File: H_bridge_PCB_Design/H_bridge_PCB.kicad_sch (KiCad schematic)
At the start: 7 parts, among them U1 ESP32-WROOM-32

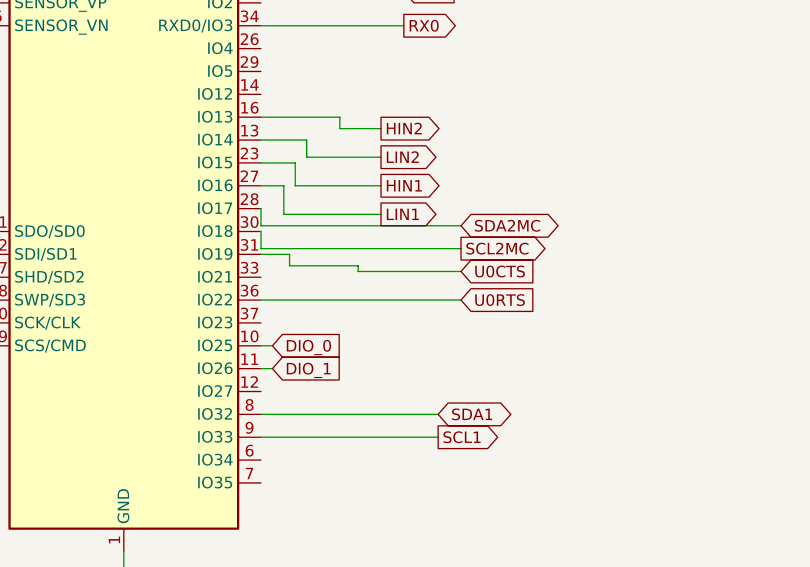
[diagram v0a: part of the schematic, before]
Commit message: Interrupt for PWM and unipolar modulation
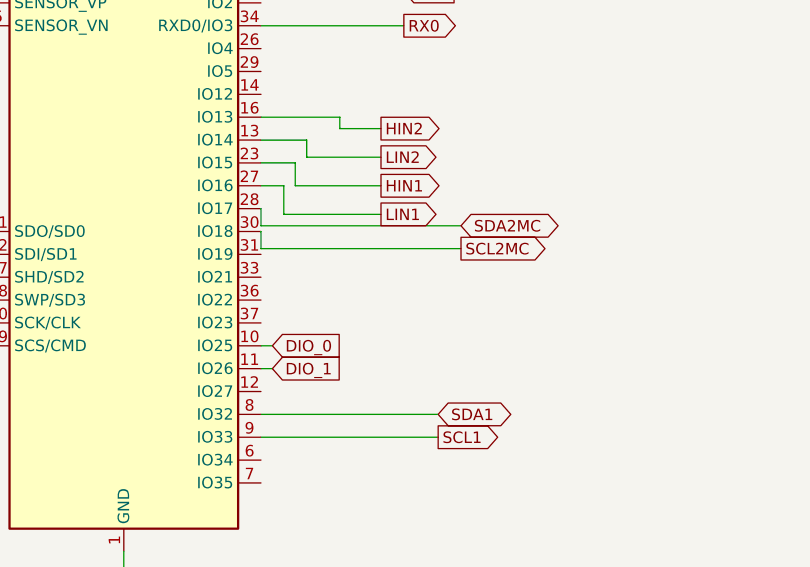
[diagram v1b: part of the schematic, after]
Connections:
- net U0CTS: no longer names the net of U1.31 (IO19)
- net U0RTS: no longer names the net of U1.36 (IO22)
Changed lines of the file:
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@@
-	(wire
-		(pts
-			(xy 208.915 217.805) (xy 208.915 218.44)
-		)
-		(stroke
-			(width 0)
-			(type default)
-		)
-	)
 	(wire
 		(pts
@@
 	(wire
 		(pts
-			(xy 201.295 217.805) (xy 208.915 217.805)
-		)
-		(stroke
-			(width 0)
-			(type default)
-		)
-	)
-	(wire
-		(pts
 			(xy 154.94 183.515) (xy 167.64 183.515)
 		)
@@
 	(wire
 		(pts
-			(xy 198.12 216.535) (xy 201.295 216.535)
-		)
-		(stroke
-			(width 0)
-			(type default)
-		)
-	)
-	(wire
-		(pts
-			(xy 208.915 218.44) (xy 220.345 218.44)
-		)
-		(stroke
-			(width 0)
-			(type default)
-		)
-	)
-	(wire
-		(pts
 			(xy 166.37 175.26) (xy 166.37 176.53)
 		)
@@
 	(wire
 		(pts
-			(xy 201.295 216.535) (xy 201.295 217.805)
-		)
-		(stroke
-			(width 0)
-			(type default)
-		)
-	)
-	(wire
-		(pts
 			(xy 198.12 186.055) (xy 206.375 186.055)
 		)
@@
 		(pts
 			(xy 203.2 205.74) (xy 203.2 203.835)
-		)
-		(stroke
-			(width 0)
-			(type default)
-		)
-	)
-	(wire
-		(pts
-			(xy 198.12 221.615) (xy 220.345 221.615)
 		)
 		(stroke
@@
 		)
 	)
-	(global_label "U0RTS"
-		(shape input)
-		(at 220.345 221.615 0)
-		(fields_autoplaced yes)
-		(effects
-			(font
-				(size 1.27 1.27)
-			)
-			(justify left)
-		)
-		(property "Intersheetrefs" "${INTERSHEET_REFS}"
-			(at 229.3173 221.615 0)
-			(effects
-				(font
-					(size 1.27 1.27)
-				)
-				(justify left)
-				(hide yes)
-			)
-		)
-	)
 	(global_label "Io0"
 		(shape input)
@@
 			(effects
 				(font
-					(size 1.27 1.27)
-				)
-				(justify left)
-				(hide yes)
-			)
-		)
-	)
-	(global_label "U0CTS"
-		(shape input)
-		(at 220.345 218.44 0)
-		(fields_autoplaced yes)
-		(effects
-			(font
-				(size 1.27 1.27)
-			)
-			(justify left)
-		)
-		(property "Intersheetrefs" "${INTERSHEET_REFS}"
-			(at 229.3173 218.44 0)
-			(effects
-				(font

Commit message: huge changes output measurement
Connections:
- net SatusLED: now reaches U1.31 (IO19)
- net DIO_0 renamed CLK_C
- net DIO_1 renamed Data_C
- net SCL2MC renamed Data_V
- net SDA2MC renamed CLK_V
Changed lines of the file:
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@@
-	(wire
-		(pts
-			(xy 198.12 229.235) (xy 199.39 229.235)
-		)
-		(stroke
-			(width 0)
-			(type default)
-		)
-	)
 	(wire
 		(pts
@@
 	(wire
 		(pts
-			(xy 198.12 213.36) (xy 220.345 213.36)
-		)
-		(stroke
-			(width 0)
-			(type default)
-		)
-	)
-	(wire
-		(pts
 			(xy 201.93 208.915) (xy 211.455 208.915)
 		)
@@
 	(wire
 		(pts
+			(xy 201.295 216.535) (xy 198.12 216.535)
+		)
+		(stroke
+			(width 0)
+			(type default)
+		)
+	)
+	(wire
+		(pts
 			(xy 207.645 179.705) (xy 207.645 183.515)
 		)
@@
 	(wire
 		(pts
-			(xy 198.12 226.695) (xy 199.39 226.695)
-		)
-		(stroke
-			(width 0)
-			(type default)
-		)
-	)
-	(wire
-		(pts
-			(xy 220.345 215.9) (xy 198.12 215.9)
+			(xy 198.12 213.36) (xy 198.12 211.455)
+		)
+		(stroke
+			(width 0)
+			(type default)
+		)
+	)
+	(wire
+		(pts
+			(xy 198.12 213.36) (xy 220.98 213.36)
 		)
 		(stroke
@@
 	(wire
 		(pts
+			(xy 198.12 215.9) (xy 219.71 215.9)
+		)
+		(stroke
+			(width 0)
+			(type default)
+		)
+	)
+	(wire
+		(pts
 			(xy 171.45 163.83) (xy 182.88 163.83)
 		)
@@
 	(wire
 		(pts
-			(xy 198.12 213.36) (xy 198.12 211.455)
+			(xy 213.36 226.695) (xy 198.12 226.695)
 		)
 		(stroke
@@
 	(wire
 		(pts
+			(xy 212.09 229.235) (xy 198.12 229.235)
+		)
+		(stroke
+			(width 0)
+			(type default)
+		)
+	)
+	(wire
+		(pts
 			(xy 201.93 206.375) (xy 198.12 206.375)
 		)
@@
 	(wire
 		(pts
+			(xy 201.295 218.44) (xy 201.295 216.535)
+		)
+		(stroke
+			(width 0)
+			(type default)
+		)
+	)
+	(wire
+		(pts
 			(xy 148.59 175.26) (xy 148.59 183.515)
 		)
@@
 		)
 	)
+	(wire
+		(pts
+			(xy 219.075 218.44) (xy 201.295 218.44)
+		)
+		(stroke
+			(width 0)
+			(type default)
+		)
+	)
 	(global_label "LIN1"
 		(shape output)
@@
 		(property "Intersheetrefs" "${INTERSHEET_REFS}"
 			(at 218.6131 212.09 0)
-			(effects
-				(font
-					(size 1.27 1.27)
-				)
-				(justify left)
-				(hide yes)
-			)
-		)
-	)
-	(global_label "DIO_1"
-		(shape input)
-		(at 199.39 229.235 0)
-		(fields_autoplaced yes)
-		(effects
-			(font
-				(size 1.27 1.27)
-			)
-			(justify left)
-		)
-		(property "Intersheetrefs" "${INTERSHEET_REFS}"
-			(at 207.7576 229.235 0)
 			(effects
 				(font
@@
 		)
 	)
-	(global_label "DIO_0"
-		(shape input)
-		(at 199.39 226.695 0)
-		(fields_autoplaced yes)
-		(effects
-			(font
-				(size 1.27 1.27)
-			)
-			(justify left)
-		)
-		(property "Intersheetrefs" "${INTERSHEET_REFS}"
-			(at 207.7576 226.695 0)
+	(global_label "CLK_V"
+		(shape output)
+		(at 220.98 213.36 0)
+		(fields_autoplaced yes)
+		(effects
+			(font
+				(size 1.27 1.27)
+			)
+			(justify left)
+		)
+		(property "Intersheetrefs" "${INTERSHEET_REFS}"
+			(at 229.5895 213.36 0)
 			(effects
 				(font
@@
 		)
 	)
-	(global_label "SCL2MC"
-		(shape output)
-		(at 220.345 215.9 0)
-		(fields_autoplaced yes)
-		(effects
-			(font
-				(size 1.27 1.27)
-			)
-			(justify left)
-		)
-		(property "Intersheetrefs" "${INTERSHEET_REFS}"
-			(at 230.7687 215.9 0)
-			(effects
-				(font
-					(size 1.27 1.27)
-				)
-				(justify left)
-				(hide yes)
-			)
-		)
-	)
-	(global_label "SDA2MC"
-		(shape bidirectional)
-		(at 220.345 213.36 0)
-		(fields_autoplaced yes)
-		(effects
-			(font
-				(size 1.27 1.27)
-			)
-			(justify left)
-		)
-		(property "Intersheetrefs" "${INTERSHEET_REFS}"
-			(at 231.9405 213.36 0)
-			(effects
-				(font
-					(size 1.27 1.27)
-				)
-				(justify left)
-				(hide yes)
-			)
-		)
-	)
 	(global_label "SCL1"
 		(shape output)
@@
 		)
 	)
+	(global_label "Data_V"
+		(shape input)
+		(at 219.71 215.9 0)
+		(fields_autoplaced yes)
+		(effects
+			(font
+				(size 1.27 1.27)
+			)
+			(justify left)
+		)
+		(property "Intersheetrefs" "${INTERSHEET_REFS}"
+			(at 229.0451 215.9 0)
+			(effects
+				(font
+					(size 1.27 1.27)
+				)
+				(justify left)
+				(hide yes)
+			)
+		)
+	)
 	(global_label "RX0"
 		(shape output)
@@
 		(property "Intersheetrefs" "${INTERSHEET_REFS}"
 			(at 220.6692 191.135 0)
+			(effects
+				(font
+					(size 1.27 1.27)
+				)
+				(justify left)
+				(hide yes)
+			)
+		)
+	)
+	(global_label "Data_C"
+		(shape input)
+		(at 212.09 229.235 0)
+		(fields_autoplaced yes)
+		(effects
+			(font
+				(size 1.27 1.27)
+			)
+			(justify left)
+		)
+		(property "Intersheetrefs" "${INTERSHEET_REFS}"
+			(at 221.6065 229.235 0)
+			(effects
+				(font
+					(size 1.27 1.27)
+				)
+				(justify left)
+				(hide yes)
+			)
+		)
+	)
+	(global_label "CLK_C"
+		(shape output)
+		(at 213.36 226.695 0)
+		(fields_autoplaced yes)
+		(effects
+			(font
+				(size 1.27 1.27)
+			)
+			(justify left)
+		)
+		(property "Intersheetrefs" "${INTERSHEET_REFS}"
+			(at 222.1509 226.695 0)
 			(effects
 				(font
@@
 			(effects
 				(font
+					(size 1.27 1.27)
+				)
+				(justify left)
+				(hide yes)
+			)
+		)
+	)
+	(global_label "SatusLED"
+		(shape output)
+		(at 219.075 218.44 0)
+		(fields_autoplaced yes)
+		(effects
+			(font
+				(size 1.27 1.27)
+			)
+			(justify left)
+		)
+		(property "Intersheetrefs" "${INTERSHEET_REFS}"
+			(at 230.7686 218.44 0)
+			(effects
+				(font

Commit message: new pcb
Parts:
- added S1: B3U-1000P, B3U-1000P, symbol SamacSysParts:B3U-1000P
- C10, C20: LCSC Part # (none) -> C49678; LCSC Part# C49678 -> (none)
- C12: LCSC Part # (none) -> C28323; LCSC Part# C28323 -> (none)
- C9: LCSC Part # (none) -> C49678; LCSC Part# C165822 -> (none)
- R13: LCSC Part # (none) -> C139925; LCSC Part# C139925 -> (none)
- R14: LCSC Part # (none) -> C2828700; LCSC Part# C2828700 -> (none)
- U1: LCSC Part # (none) -> C701343; LCSC Part# C701343 -> (none)
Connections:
- net EN: now also S1.2 (A)
- net GND: now also S1.1 (K)
- net Shutoff1: now reaches U1.33 (IO21)
- net SatusLED renamed StatusLED
